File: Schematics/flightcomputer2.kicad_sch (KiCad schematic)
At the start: 0 parts

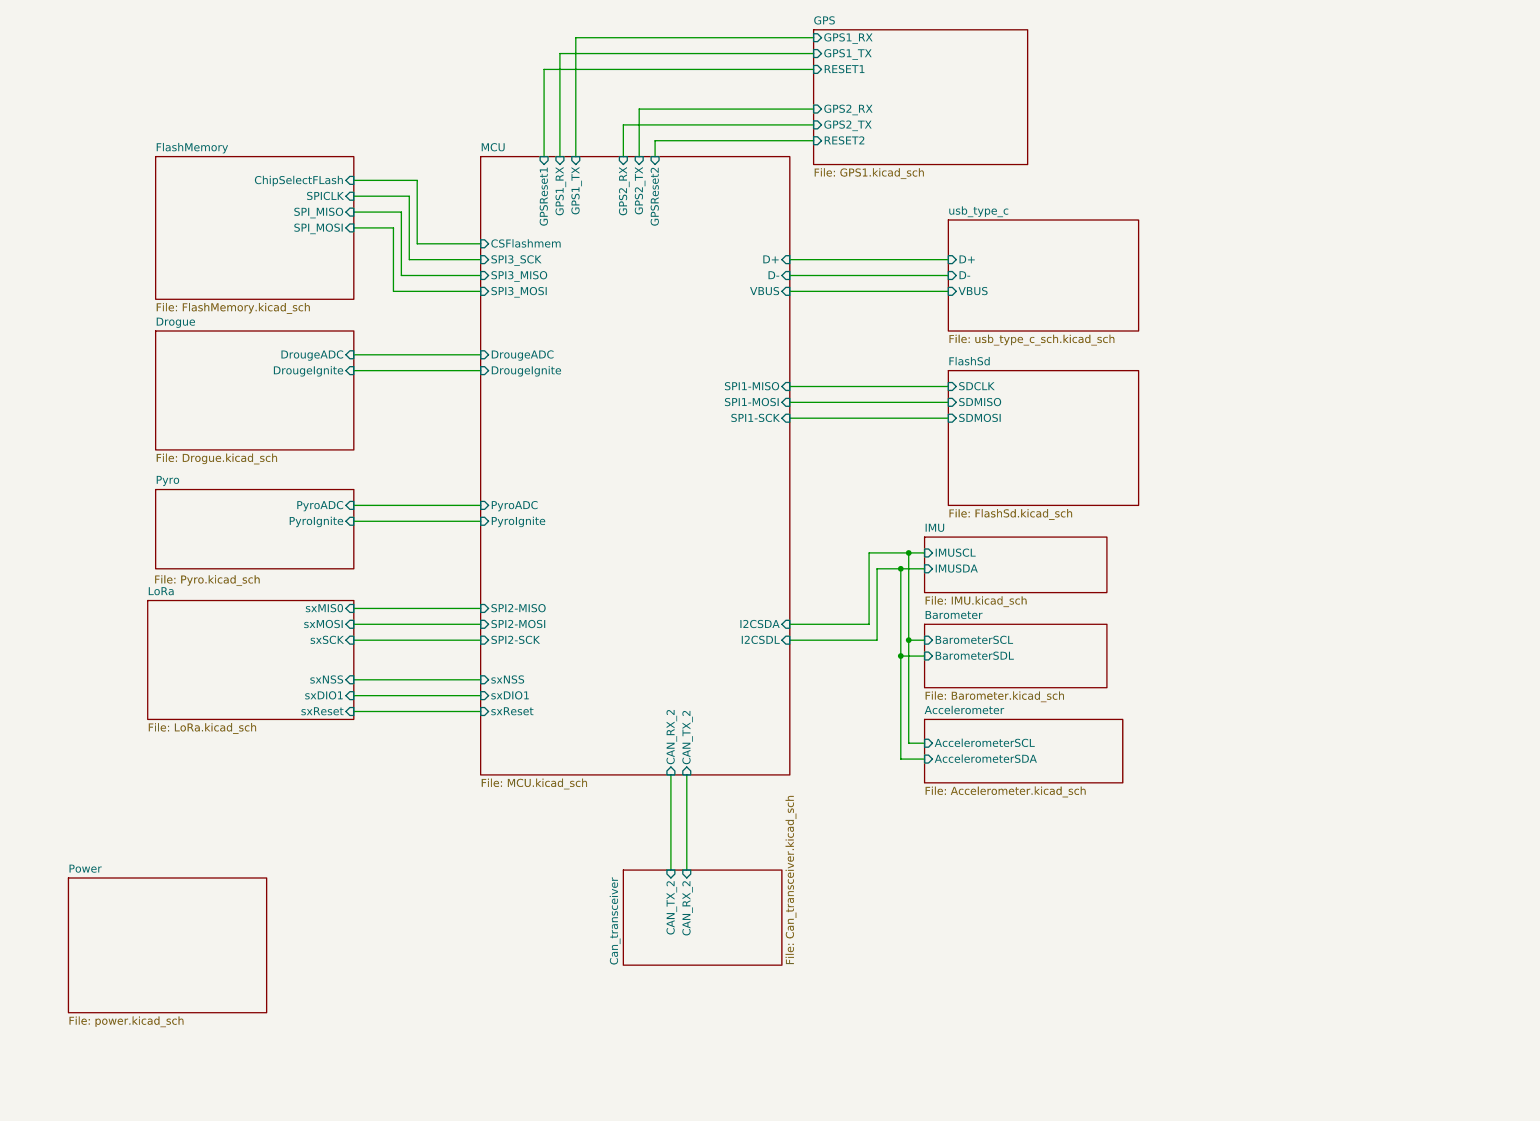
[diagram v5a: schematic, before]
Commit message: added aux pyro added reverse polarity protection re routed just need to clean up and check pin assignments
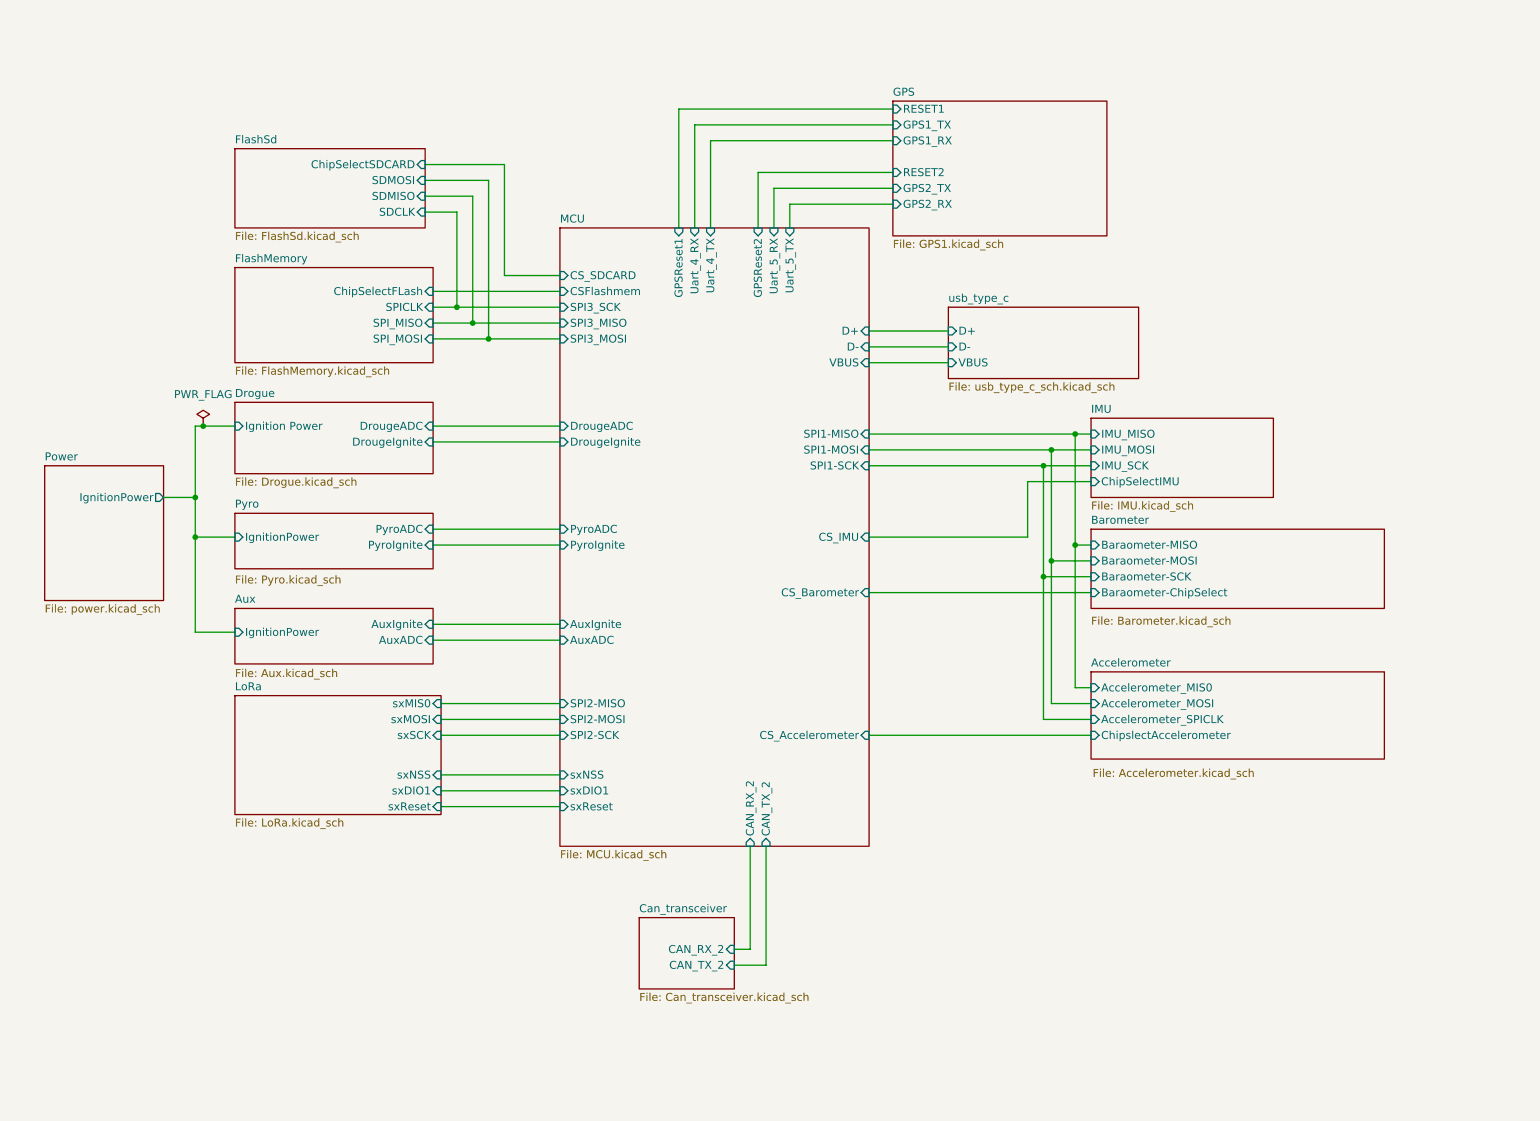
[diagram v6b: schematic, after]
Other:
- added sheet Aux (Aux.kicad_sch)
- sheet Accelerometer ports: added Accelerometer_MIS0, Accelerometer_MOSI, Accelerometer_SPICLK, ChipslectAccelerometer; removed AccelerometerSCL, AccelerometerSDA
- sheet Barometer ports: added Baraometer-ChipSelect, Baraometer-MISO, Baraometer-MOSI, Baraometer-SCK; removed BarometerSCL, BarometerSDL
- sheet Drogue ports: added Ignition Power; removed none
- sheet FlashSd ports: added ChipSelectSDCARD; removed none
- sheet IMU ports: added ChipSelectIMU, IMU_MISO, IMU_MOSI, IMU_SCK; removed IMUSCL, IMUSDA
- sheet MCU ports: added AuxADC, AuxIgnite, CS_Accelerometer, CS_Barometer, CS_IMU, CS_SDCARD, Uart_4_RX, Uart_4_TX, Uart_5_RX, Uart_5_TX; removed GPS1_RX, GPS1_TX, GPS2_RX, GPS2_TX, I2CSDA, I2CSDL
- sheet Power ports: added IgnitionPower; removed none
- sheet Pyro ports: added IgnitionPower; removed none

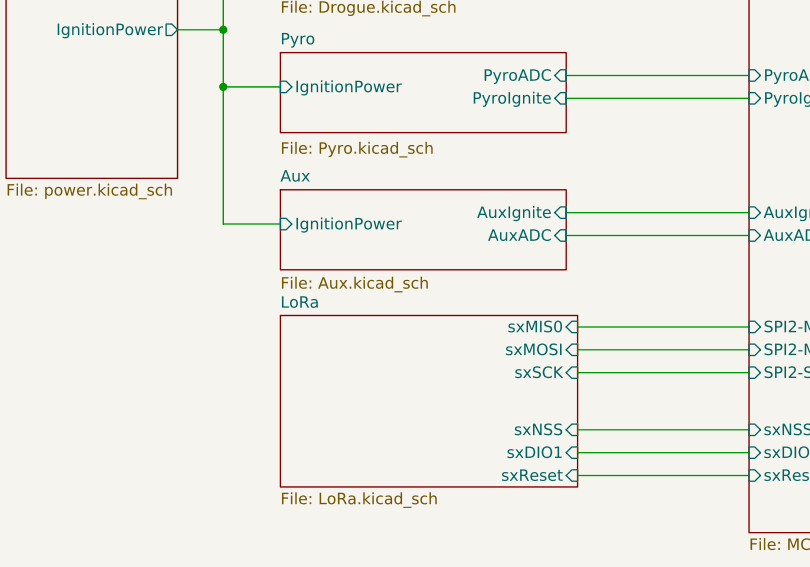
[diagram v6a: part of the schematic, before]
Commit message: layout completed added testpoints and verified mosfet ect
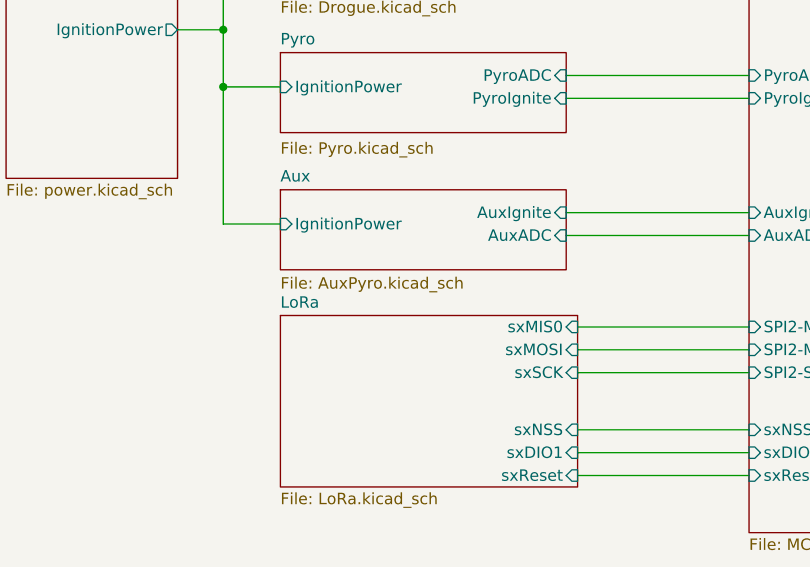
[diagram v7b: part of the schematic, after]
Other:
- sheet Aux: file Aux.kicad_sch -> AuxPyro.kicad_sch
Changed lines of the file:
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@@
 			)
 		)
-		(property "Sheetfile" "Aux.kicad_sch"
+		(property "Sheetfile" "AuxPyro.kicad_sch"
 			(at 59.69 120.142 0)
 			(effects

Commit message: added comments, awaiting review
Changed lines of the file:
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@@
-	)
-	(junction
-		(at 54.61 81.28)
-		(diameter 0)
-		(color 0 0 0 0)
 	)
 	(junction
@@
 	)
 	(junction
+		(at 53.34 81.28)
+		(diameter 0)
+		(color 0 0 0 0)
+	)
+	(junction
 		(at 190.5 102.87)
 		(diameter 0)
@@
 	(wire
 		(pts
+			(xy 53.34 81.28) (xy 59.69 81.28)
+		)
+		(stroke
+			(width 0)
+			(type default)
+		)
+	)
+	(wire
+		(pts
 			(xy 91.44 64.77) (xy 97.79 64.77)
 		)
@@
 	(wire
 		(pts
-			(xy 53.34 81.28) (xy 54.61 81.28)
-		)
-		(stroke
-			(width 0)
-			(type default)
-		)
-	)
-	(wire
-		(pts
 			(xy 92.71 142.24) (xy 111.76 142.24)
 		)
@@
 		(pts
 			(xy 161.29 87.63) (xy 189.23 87.63)
-		)
-		(stroke
-			(width 0)
-			(type default)
-		)
-	)
-	(wire
-		(pts
-			(xy 54.61 81.28) (xy 59.69 81.28)
 		)
 		(stroke
@@
 	(symbol
 		(lib_id "power:PWR_FLAG")
-		(at 54.61 81.28 0)
+		(at 53.34 81.28 0)
 		(unit 1)
 		(exclude_from_sim no)
@@
 		(fields_autoplaced yes)
 		(property "Reference" "#FLG06"
-			(at 54.61 79.375 0)
+			(at 53.34 79.375 0)
 			(effects
 				(font
@@
 		)
 		(property "Value" "PWR_FLAG"
-			(at 54.61 76.2 0)
+			(at 53.34 76.2 0)
 			(effects
 				(font
@@
 		)
 		(property "Footprint" ""
-			(at 54.61 81.28 0)
+			(at 53.34 81.28 0)
 			(effects
 				(font
@@
 		)
 		(property "Datasheet" "~"
-			(at 54.61 81.28 0)
+			(at 53.34 81.28 0)
 			(effects
 				(font
@@
 		)
 		(property "Description" "Special symbol for telling ERC where power comes from"
-			(at 54.61 81.28 0)
+			(at 53.34 81.28 0)
 			(effects
 				(font
